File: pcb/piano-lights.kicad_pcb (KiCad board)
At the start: 2 copper layers, 98 x 48 mm, 35 parts, among them J1 FTDI RS232, J2 USB_B_Micro, J3 LED Strip, J4 AVR-ISP-6, J5 MIDI IN, J6 MIDI THRU, J7 MIDI Coupler Out, J8 MIDI Coupler In, SW2 Reset, U1 ATmega328P-P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

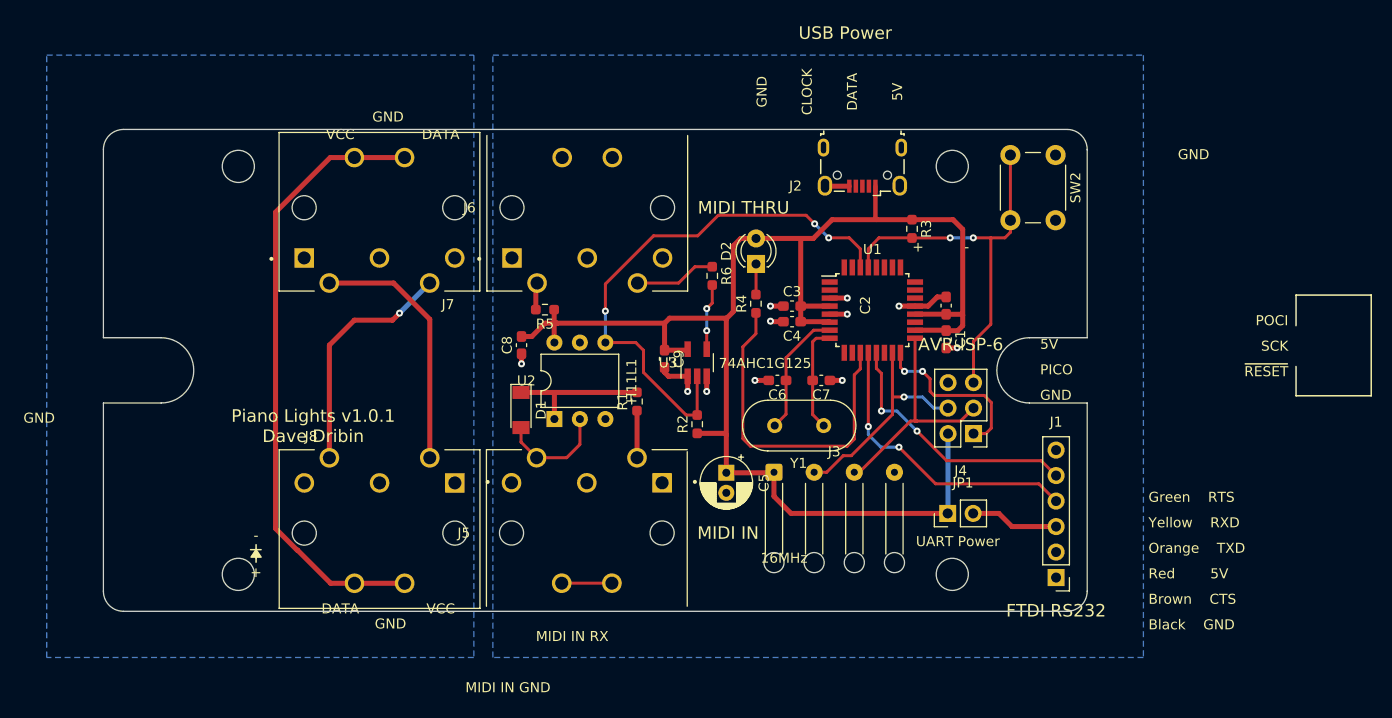
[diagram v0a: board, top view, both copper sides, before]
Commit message: Add the button back, but on a different pin. Start cleaning up silkscreen
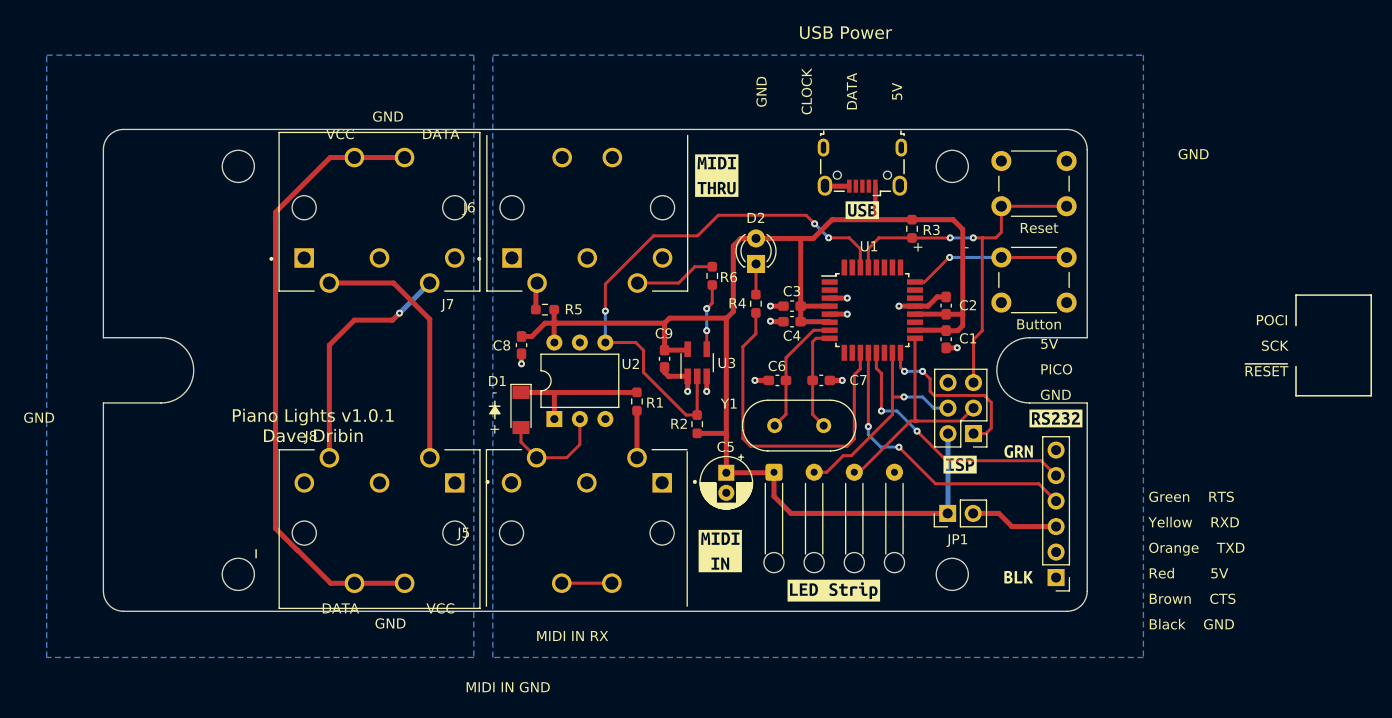
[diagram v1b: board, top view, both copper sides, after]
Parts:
- added SW1: Button, Button_Switch_THT:SW_PUSH_6mm_H5mm, F.Cu at (175.8, 79.8)
- added kibuzzard-63E9D0C7: G***, kibuzzard-63E9D0C7, F.Cu at (147.5, 71.6)
- added kibuzzard-63E9D0F2: G***, kibuzzard-63E9D0F2, F.Cu at (147.8, 109.0)
- added kibuzzard-63E9D20D: G***, kibuzzard-63E9D20D, F.Cu at (181.3, 95.8)
- added kibuzzard-63E9D252: G***, kibuzzard-63E9D252, F.Cu at (159.2, 112.9)
- added kibuzzard-63E9D28E: G***, kibuzzard-63E9D28E, F.Cu at (177.6, 99.1)
- added kibuzzard-63E9D296: G***, kibuzzard-63E9D296, F.Cu at (177.6, 111.6)
- added kibuzzard-63E9D2D7: G***, kibuzzard-63E9D2D7, F.Cu at (171.7, 100.4)
- added kibuzzard-63E9D34A: G***, kibuzzard-63E9D34A, F.Cu at (162.0, 75.0)
- moved SW2 5.43 mm to (175.8, 70.2), turned to 0 degrees
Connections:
- U1 pad 24: unconnected-(U1-Pad24) -> /Button
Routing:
- net /Button: track 0.00 -> 16.1 mm, vias 0 -> 1

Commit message: Finish cleaning up silkscreen. Passes DRC. Add dimensions.
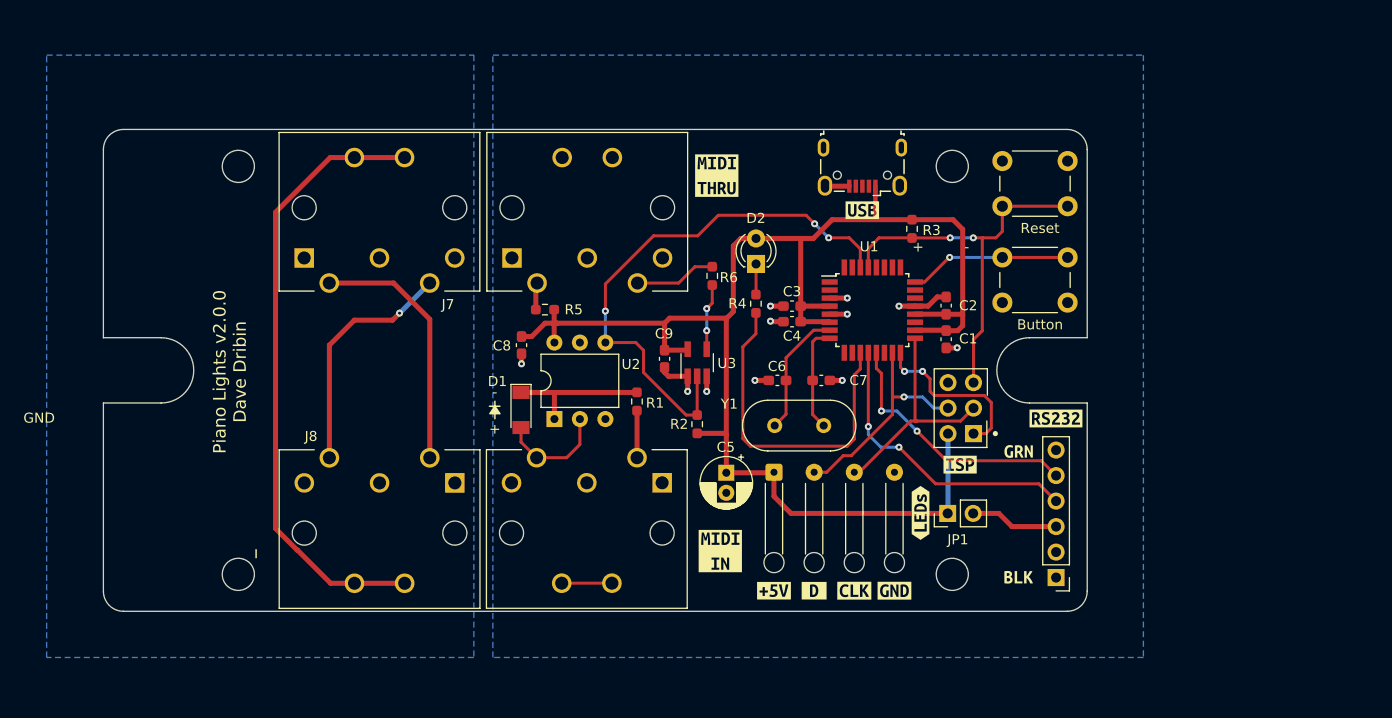
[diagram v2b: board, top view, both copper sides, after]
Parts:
- removed kibuzzard-63E9D252: G***, kibuzzard-63E9D252
- added kibuzzard-63E9D435: G***, kibuzzard-63E9D435, F.Cu at (153.2, 113.0)
- added kibuzzard-63E9D44E: G***, kibuzzard-63E9D44E, F.Cu at (165.2, 113.0)
- added kibuzzard-63E9D473: G***, kibuzzard-63E9D473, F.Cu at (167.8, 105.2)
- added kibuzzard-63E9D50C: G***, kibuzzard-63E9D50C, F.Cu at (161.2, 113.0)
- added kibuzzard-63E9D543: G***, kibuzzard-63E9D543, F.Cu at (157.2, 113.0)
- moved SW1 0.10 mm to (175.9, 79.8)
- moved SW2 0.10 mm to (175.9, 70.2)
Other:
- board text added: "Piano Lights v2.0.0 Dave Dribin"
- board text removed: "5V"
- board text removed: "Black GND"
- board text removed: "Brown CTS"
- board text removed: "CLOCK"
- board text removed: "DATA"
- board text removed: "Green RTS"
- board text removed: "MIDI IN GND"
- board text removed: "MIDI IN RX"
- board text removed: "Orange TXD"
- board text removed: "PICO"
- board text removed: "POCI"
- board text removed: "Piano Lights v1.0.1 Dave Dribin"
- board text removed: "Red 5V"
- board text removed: "SCK"
- board text removed: "USB Power"
- board text removed: "VCC"
- board text removed: "Yellow RXD"
- board text removed: "~{RESET}"

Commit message: Last silkscreen tweaks
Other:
- board text removed: "GND"
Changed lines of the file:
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@@
       (drillshape 0)
       (scaleselection 1)
-      (outputdirectory "gerbers/")
+      (outputdirectory "output/gerbers/")
     )
   )
@@
     (attr board_only exclude_from_pos_files exclude_from_bom)
     (fp_text reference "kibuzzard-63E9D473" (at 0 -3.92807 90) (layer "F.SilkS") hide
-      (effects (font (size 0 0)))
+      (effects (font (size 0 0) (thickness 0.15)))
     )
     (fp_text value "G***" (at 0 3.92807 90) (layer "F.SilkS") hide
-      (effects (font (size 0 0)))
+      (effects (font (size 0 0) (thickness 0.15)))
     )
     (fp_poly (pts
@@
     (attr board_only exclude_from_pos_files exclude_from_bom)
     (fp_text reference "kibuzzard-63E9D435" (at 0 -3.923109) (layer "F.SilkS") hide
-      (effects (font (size 0 0)))
+      (effects (font (size 0 0) (thickness 0.15)))
     )
     (fp_text value "G***" (at 0 3.923109) (layer "F.SilkS") hide
-      (effects (font (size 0 0)))
+      (effects (font (size 0 0) (thickness 0.15)))
     )
     (fp_poly (pts
@@
     (attr board_only exclude_from_pos_files exclude_from_bom)
     (fp_text reference "kibuzzard-63E9D543" (at 0 -3.925094) (layer "F.SilkS") hide
-      (effects (font (size 0 0)))
+      (effects (font (size 0 0) (thickness 0.15)))
     )
     (fp_text value "G***" (at 0 3.925094) (layer "F.SilkS") hide
-      (effects (font (size 0 0)))
+      (effects (font (size 0 0) (thickness 0.15)))
     )
     (fp_poly (pts
@@
     (attr board_only exclude_from_pos_files exclude_from_bom)
     (fp_text reference "kibuzzard-63E9D50C" (at 0 -3.937) (layer "F.SilkS") hide
-      (effects (font (size 0 0)))
+      (effects (font (size 0 0) (thickness 0.15)))
     )
     (fp_text value "G***" (at 0 3.937) (layer "F.SilkS") hide
-      (effects (font (size 0 0)))
+      (effects (font (size 0 0) (thickness 0.15)))
     )
     (fp_poly (pts
@@
     (attr board_only exclude_from_pos_files exclude_from_bom)
     (fp_text reference "kibuzzard-63E9D44E" (at 0 -3.937) (layer "F.SilkS") hide
-      (effects (font (size 0 0)))
+      (effects (font (size 0 0) (thickness 0.15)))
     )
     (fp_text value "G***" (at 0 3.937) (layer "F.SilkS") hide
-      (effects (font (size 0 0)))
+      (effects (font (size 0 0) (thickness 0.15)))
     )
     (fp_poly (pts
@@
     (pad "" np_thru_hole circle (at 0 9) (size 2 2) (drill 2) (layers *.Cu *.Mask))
     (pad "" np_thru_hole circle (at 8 9) (size 2 2) (drill 2) (layers *.Cu *.Mask))
-    (pad "1" thru_hole roundrect (at 0 0) (size 1.7 1.7) (drill 0.7) (layers *.Cu *.Mask) (roundrect_rratio 0.147059)
+    (pad "1" thru_hole roundrect (at 0 0) (size 1.7 1.7) (drill 0.7) (layers *.Cu *.Mask) (roundrect_rratio 0.1470588235)
       (net 4 "+5V") (pinfunction "Pin_1") (pintype "passive"))
     (pad "2" thru_hole circle (at 4 0) (size 1.7 1.7) (drill 0.7) (layers *.Cu *.Mask)
@@
     (effects (font (size 1 1) (thickness 0.15)))
   )
-  (gr_text "GND" (at 80 95.75) (layer "F.SilkS")
-    (effects (font (size 1 1) (thickness 0.15)))
-  )

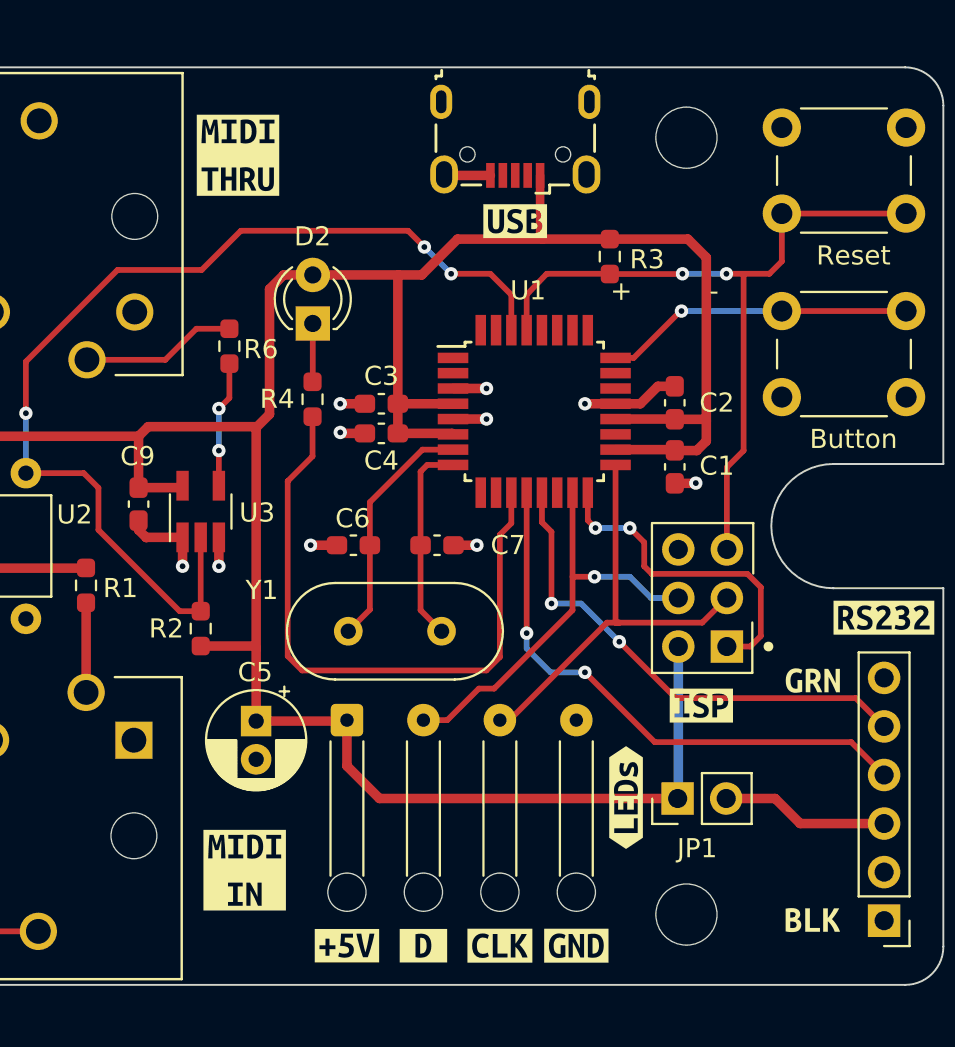
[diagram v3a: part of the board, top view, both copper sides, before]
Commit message: Reroute /LED signal away from the crystal
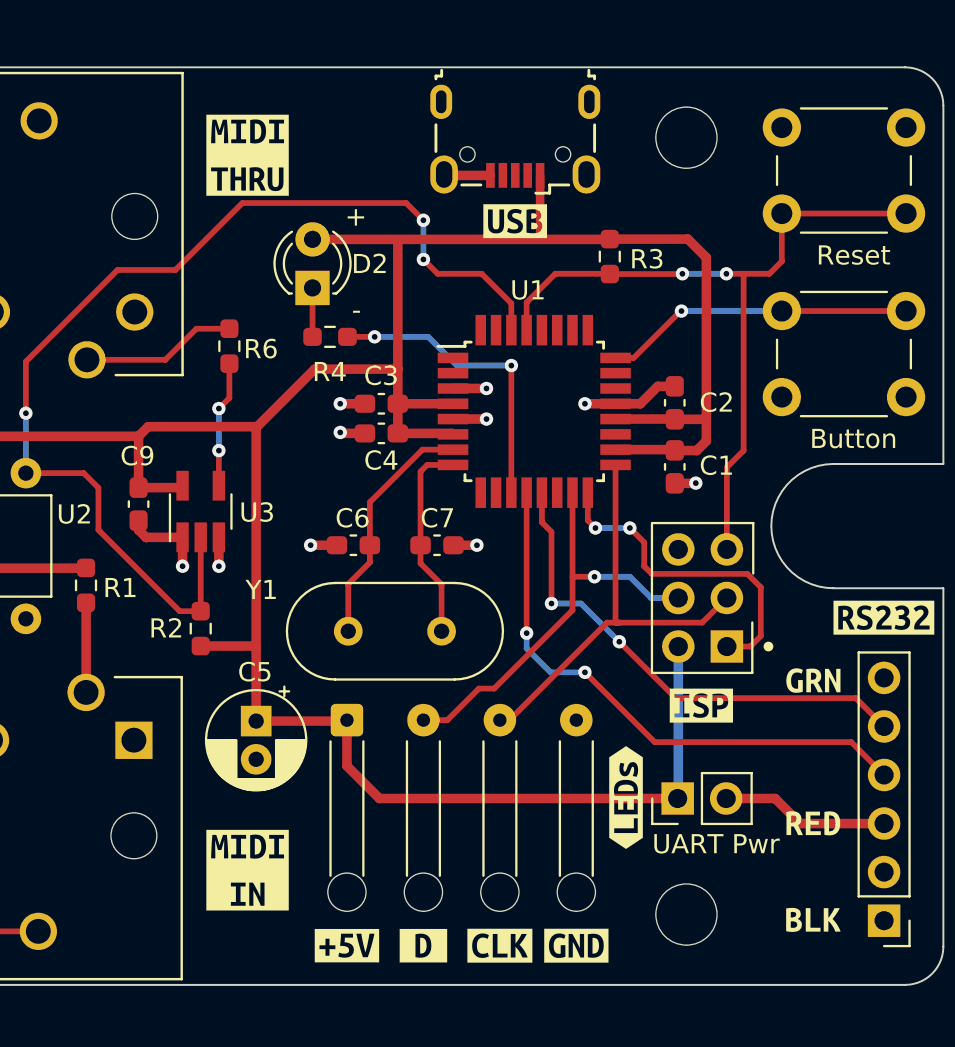
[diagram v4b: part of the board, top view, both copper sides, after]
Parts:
- added kibuzzard-63EA7125: G***, kibuzzard-63EA7125, F.Cu at (177.6, 106.5)
- JP1: value UART Power -> UART Pwr
- moved R4 3.39 mm to (152.3, 81.1), turned to 180 degrees
- moved D2 1.86 mm to (151.4, 78.5)
- moved kibuzzard-63E9D0C7 0.50 mm to (148.0, 71.6)
- moved kibuzzard-63E9D0F2 0.15 mm to (148.0, 109.0)
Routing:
- net /~{LED}: track 33.6 -> 15.8 mm, vias 0 -> 2
- net /MIDI_RX: track 54.6 -> 56.7 mm
- net +5V: track 150.0 -> 149.3 mm

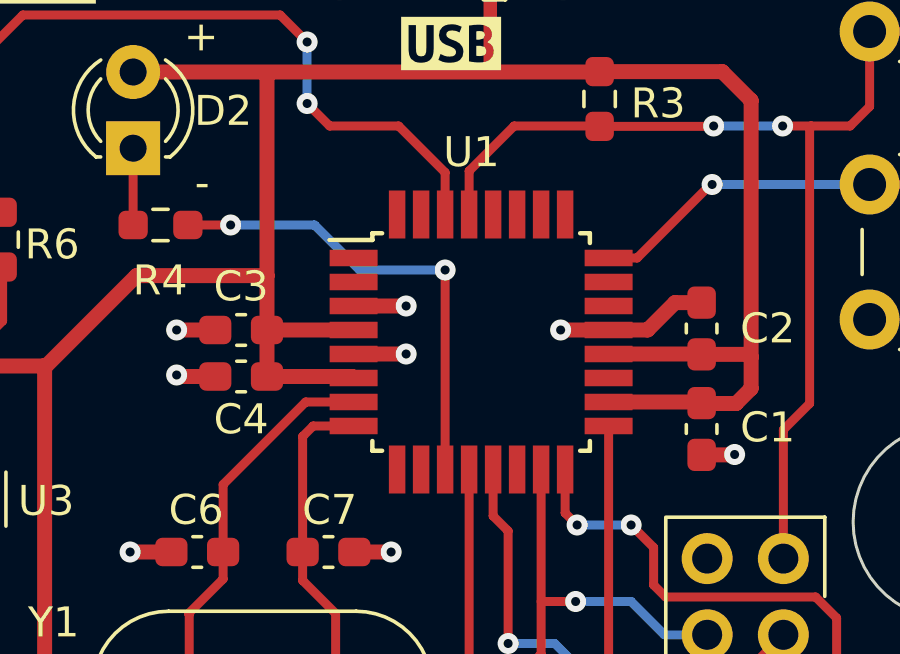
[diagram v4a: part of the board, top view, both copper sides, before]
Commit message: Move /LED to Pin 1 for easier PCB routing
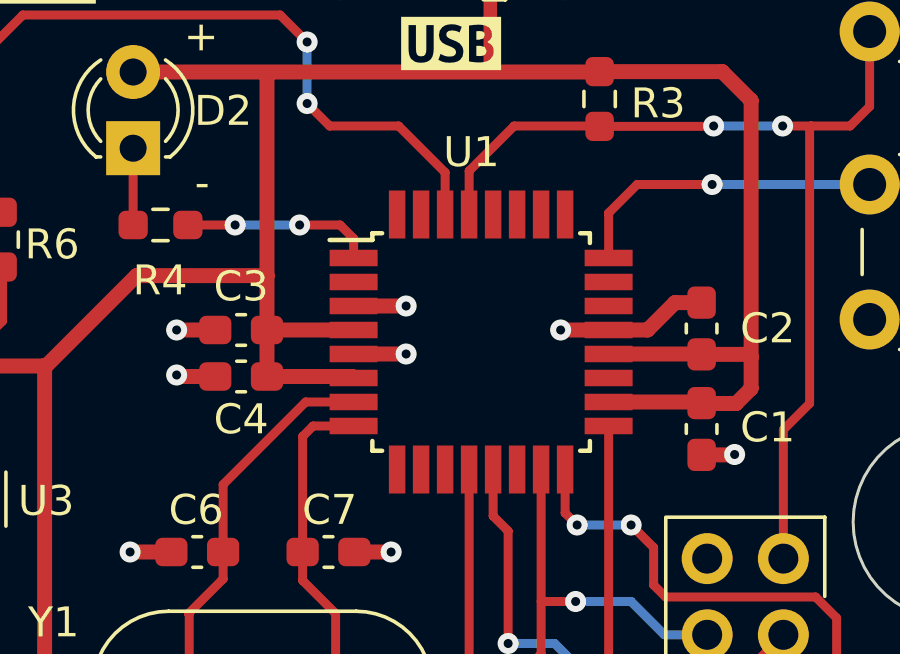
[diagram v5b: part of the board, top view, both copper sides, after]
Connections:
- U1 pad 1: unconnected-(U1-Pad1) -> /~{LED}
- U1 pad 11: /~{LED} -> unconnected-(U1-Pad11)
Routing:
- net /~{LED}: track 15.8 -> 6.36 mm
- net /Button: track 16.2 -> 17.1 mm
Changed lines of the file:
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@@
   (net 26 "unconnected-(J5-Pad1)")
   (net 27 "unconnected-(J6-Pad1)")
-  (net 28 "unconnected-(U1-Pad1)")
+  (net 28 "unconnected-(U1-Pad11)")
   (net 29 "/MIDI_RX")
   (net 30 "unconnected-(U2-Pad3)")
@@
     (attr board_only exclude_from_pos_files exclude_from_bom)
     (fp_text reference "kibuzzard-63EA7125" (at 0 -3.677047) (layer "F.SilkS") hide
-      (effects (font (size 0 0)))
+      (effects (font (size 0 0) (thickness 0.15)))
     )
     (fp_text value "G***" (at 0 3.677047) (layer "F.SilkS") hide
-      (effects (font (size 0 0)))
+      (effects (font (size 0 0) (thickness 0.15)))
     )
     (fp_poly (pts
@@
     (fp_line (start 3.5 3.5) (end -3.5 3.5) (layer "F.Fab") (width 0.15))
     (pad "1" smd rect (at -4.25 -2.8) (size 1.6 0.55) (layers "F.Cu" "F.Paste" "F.Mask")
-      (net 28 "unconnected-(U1-Pad1)") (pinfunction "D3/PD3") (pintype "bidirectional+no_connect"))
+      (net 32 "/~{LED}") (pinfunction "D3/PD3") (pintype "bidirectional"))
     (pad "2" smd rect (at -4.25 -2) (size 1.6 0.55) (layers "F.Cu" "F.Paste" "F.Mask")
       (net 33 "unconnected-(U1-Pad2)") (pinfunction "D4/PD4") (pintype "bidirectional+no_connect"))
@@
       (net 35 "unconnected-(U1-Pad10)") (pinfunction "D6/PD6") (pintype "bidirectional+no_connect"))
     (pad "11" smd rect (at -1.2 4.25 90) (size 1.6 0.55) (layers "F.Cu" "F.Paste" "F.Mask")
-      (net 32 "/~{LED}") (pinfunction "D7/PD7") (pintype "bidirectional"))
+      (net 28 "unconnected-(U1-Pad11)") (pinfunction "D7/PD7") (pintype "bidirectional+no_connect"))
     (pad "12" smd rect (at -0.4 4.25 90) (size 1.6 0.55) (layers "F.Cu" "F.Paste" "F.Mask")
       (net 24 "/DEBUG_RX") (pinfunction "D8/PB0") (pintype "bidirectional"))
@@
   (via (at 146.5 84.85) (size 0.7) (drill 0.3) (layers "F.Cu" "B.Cu") (net 31))
   (segment (start 146.5 87.05) (end 146.5 84.85) (width 0.3) (layer "B.Cu") (net 31))
-  (segment (start 154.65 81.1) (end 153.225 81.1) (width 0.3) (layer "F.Cu") (net 32))
-  (segment (start 161.8 89.25) (end 161.8 82.6) (width 0.3) (layer "F.Cu") (net 32))
-  (via (at 154.65 81.1) (size 0.7) (drill 0.3) (layers "F.Cu" "B.Cu") (net 32))
-  (via (at 161.8 82.6) (size 0.7) (drill 0.3) (layers "F.Cu" "B.Cu") (net 32))
-  (segment (start 158.95 82.6) (end 157.45 81.1) (width 0.3) (layer "B.Cu") (net 32))
-  (segment (start 161.8 82.6) (end 158.95 82.6) (width 0.3) (layer "B.Cu") (net 32))
-  (segment (start 157.45 81.1) (end 154.65 81.1) (width 0.3) (layer "B.Cu") (net 32))
-  (segment (start 167.25 82.2) (end 168.2 82.2) (width 0.3) (layer "F.Cu") (net 40))
-  (segment (start 170.65 79.75) (end 170.7 79.75) (width 0.3) (layer "F.Cu") (net 40))
-  (segment (start 168.2 82.2) (end 170.65 79.75) (width 0.3) (layer "F.Cu") (net 40))
+  (segment (start 154.8 81.1) (end 153.225 81.1) (width 0.3) (layer "F.Cu") (net 32))
+  (segment (start 158.75 81.55) (end 158.75 82.2) (width 0.3) (layer "F.Cu") (net 32))
+  (segment (start 158.3 81.1) (end 158.75 81.55) (width 0.3) (layer "F.Cu") (net 32))
+  (segment (start 156.95 81.1) (end 158.3 81.1) (width 0.3) (layer "F.Cu") (net 32))
+  (via (at 156.95 81.1) (size 0.7) (drill 0.3) (layers "F.Cu" "B.Cu") (net 32))
+  (via (at 154.8 81.1) (size 0.7) (drill 0.3) (layers "F.Cu" "B.Cu") (net 32))
+  (segment (start 156.95 81.1) (end 154.8 81.1) (width 0.3) (layer "B.Cu") (net 32))
+  (segment (start 168.2 79.75) (end 170.7 79.75) (width 0.3) (layer "F.Cu") (net 40))
+  (segment (start 167.25 80.7) (end 168.2 79.75) (width 0.3) (layer "F.Cu") (net 40))
+  (segment (start 167.25 82.2) (end 167.25 80.7) (width 0.3) (layer "F.Cu") (net 40))
   (segment (start 175.95 79.75) (end 182.45 79.75) (width 0.3) (layer "F.Cu") (net 40))
   (via (at 170.7 79.75) (size 0.7) (drill 0.3) (layers "F.Cu" "B.Cu") (net 40))
